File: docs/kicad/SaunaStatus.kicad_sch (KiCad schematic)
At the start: 9 parts, among them J1 PT1000-Connector, J2 28BYJ-48, J3 28BYJ-48, U1 ESP32-WROOM-32, U2 MAX31865xAP, U3 DHT21/AM2301, U4 DHT21/AM2301, U5 ULN2003A, U6 ULN2003A

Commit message: Replace INA219 power monitor with INA260 throughout
- src/main.cpp: swap Adafruit_INA219 → Adafruit_INA260; update include,
  defines (INA219_* → INA260_*), object name (ina219 → ina260),
  init guard (ina219_ok → ina260_ok), and all read methods
  (getPowerW/getShuntVoltage_mV → readPower/readCurrent/readBusVoltage)
- platformio.ini: replace INA219 library with
  adafruit/Adafruit INA260 Library@^1.5.3
- docs/hardware-rules.md: update Pin Table, Section 3 (I2C Bus),
  Section 7 (Power Monitor), constraint #9, Section 11 sauna note,
  and Schematic Component Reference table (U7 entry)
- docs/config-reference.md: rename INA219_SDA/SCL → INA260_SDA/SCL
- docs/api-reference.md: update pvolt/pcurr/pmw descriptions, MQTT
  field table, and InfluxDB sauna_status fields; fix gateway to 192.168.1.100
- docs/pinout.md: add INA260 I2C wiring section; add GPIO 4/13 to
  Quick Reference table
- CLAUDE.md: update project overview, Sensor Layer table,
  WebSocket JSON schema, and InfluxDB field descriptions
- docs/kicad/SaunaStatus.kicad_sch: add INA260 (U7, TSSOP-16) component

INA260 wiring: SDA=GPIO4, SCL=GPIO13, A0=A1=GND (I2C address 0x40).
Integrated 2 mΩ shunt — no external shunt resistor required.
U7 is placed in the schematic but not yet wired; connections must be
routed in the next PCB revision.

Co-Authored-By: Claude Sonnet 4.6 <noreply@anthropic.com>
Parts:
- added U7: INA260, Package_SO:TSSOP-16_4.4x5mm_P0.65mm, symbol Sensor:INA260
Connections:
- new net: U7.1 (IN+), U7.2 (IN+), U7.3 (IN+)
- new net: U7.11 (GND), U7.6 (GND)
- new net: U7.14 (IN-), U7.15 (IN-), U7.16 (IN-)
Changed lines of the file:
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@@
+	)
+	(symbol
+		(lib_id "Sensor:INA260")
+		(at 223.52 172.72 0)
+		(unit 1)
+		(exclude_from_sim no)
+		(in_bom yes)
+		(on_board yes)
+		(dnp no)
+		(fields_autoplaced yes)
+		(property "Reference" "U7"
+			(at 225.6633 160.02 0)
+			(effects
+				(font
+					(size 1.27 1.27)
+				)
+				(justify left)
+			)
+		)
+		(property "Value" "INA260"
+			(at 225.6633 162.56 0)
+			(effects
+				(font
+					(size 1.27 1.27)
+				)
+				(justify left)
+			)
+		)
+		(property "Footprint" "Package_SO:TSSOP-16_4.4x5mm_P0.65mm"
+			(at 223.52 187.96 0)
+			(effects
+				(font
+					(size 1.27 1.27)
+				)
+				(hide yes)
+			)
+		)
+		(property "Datasheet" "http://www.ti.com/lit/ds/symlink/ina260.pdf"
+			(at 223.52 175.26 0)
+			(effects
+				(font
+					(size 1.27 1.27)
+				)
+				(hide yes)
+			)
+		)
+		(property "Description" "Current/power/voltage monitor with Integrated 2mΩ Shunt Resistor, 2.7V - 5.5V, I2C, TSSOP-16"
+			(at 223.52 172.72 0)
+			(effects
+				(font
+					(size 1.27 1.27)
+				)
+				(hide yes)
+			)
+		)
+		(pin "4"
+		)
+		(pin "9"
+		)
+		(pin "12"
+		)
+		(pin "14"
+		)
+		(pin "15"
+		)
+		(pin "16"
+		)
+		(pin "7"
+		)
+		(pin "6"
+		)
+		(pin "10"
+		)
+		(pin "3"
+		)
+		(pin "2"
+		)
+		(pin "1"
+		)
+		(pin "8"
+		)
+		(pin "5"
+		)
+		(pin "13"
+		)
+		(pin "11"
+		)
+		(instances
+			(project "SaunaStatus"
+				(path "/d19a36c6-5583-4c95-873e-3cdaa80a72d5"
+					(reference "U7")
+					(unit 1)
+				)
+			)
+		)
 	)
 	(symbol

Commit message: feat(kicad): replace DHT21 sensor footprints with J4/J5 connectors
Sensors are external packages; replace U3/U4 (wrong Sensor:DHT11
footprint) with Conn_01x04 connectors matching AM2301 pinout directly:
Pin1=VDD, Pin2=DATA, Pin3=NC, Pin4=GND.

Also wire INA260 (U7): I2C_SDA/SCL to ESP32 IO4/IO13, VS→+3V3, GND,
A0/A1→GND (address 0x40), VBUS→IN+, INA_IN+/- labels for sense path.

Update PCB footprints, CLAUDE.md, and docs/pinout.md accordingly.

Co-Authored-By: Claude Sonnet 4.6 <noreply@anthropic.com>
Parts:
- removed U3, U4: DHT21/AM2301, Sensor:Aosong_DHT11_5.5x12.0_P2.54mm, symbol Sensor:DHT11
- added J4: DHT21/AM2301 Ceiling, Connector_PinHeader_2.54mm:PinHeader_1x04_P2.54mm_Vertical, symbol Connector_Generic:Conn_01x04
- added J5: DHT21/AM2301 Bench, Connector_PinHeader_2.54mm:PinHeader_1x04_P2.54mm_Vertical, symbol Connector_Generic:Conn_01x04
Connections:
- net +3V3: now also U7.10 (VS)
- net DHT_BENCH: now also J5.2 (Pin_2)
- net DHT_CEILING: now also J4.2 (Pin_2)
- net GND: now also U7.11 (GND), U7.4 (A1), U7.5 (A0), U7.6 (GND)
- net U6_28BYJ_A: no longer J3.1 (Pin_1), U6.16 (O1)
- net U6_28BYJ_B: no longer J3.2 (Pin_2), U6.15 (O2)
- net I2C_SCL: now reaches U1.16 (IO13)
- net I2C_SCL: now also U7.9 (SCL)
- net I2C_SDA: now reaches U1.26 (IO4)
- net I2C_SDA: now also U7.8 (SDA)
- net INA_IN+: now reaches U7.1 (IN+), U7.2 (IN+), U7.3 (IN+)
- net INA_IN+: now also U7.12 (VBUS)
- net INA_IN-: now reaches U7.14 (IN-), U7.15 (IN-), U7.16 (IN-)
- no-connect marks 36 -> 37

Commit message: fix(kicad): resolve ERC/DRC errors — wire J4/J5 power pins, U6 outputs, add board outline
ERC fixes (16 errors → expected 4 or fewer):
- J4 (DHT Ceiling connector): add +3V3→Pin1 and Pin4→GND wires
- J5 (DHT Bench connector): add +3V3→Pin1 and Pin4→GND wires
- Remove two dangling data-stub wires left from DHT21→connector replacement
- U6 O1/O2: add wires (162.56→182.88mm) connecting Pin16/15 to J3 Pin1/2
  via U6_28BYJ_A/B labels — mirrors the working C/D pattern

DRC fix:
- Add Edge.Cuts board outline (gr_rect 67,55 → 220,130mm) — no outline existed

Remaining DRC items require KiCad GUI:
- 49 unconnected pads: PCB has 0 routed traces, full layout required
- SSOP-20 (MAX31865) clearance violations: inherent to 0.65mm pitch, use local override
- ESP32 thermal pad 0.2mm vias: violate 0.3mm default min-drill; select fab supporting micro-vias
- Library footprint mismatches: warnings only, accept or re-sync from library

gitignore: add docs/kicad/*.rpt (ERC/DRC reports are generated, not source-controlled)

Co-Authored-By: Claude Sonnet 4.6 <noreply@anthropic.com>
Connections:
- net +3V3: now also J4.1 (Pin_1), J5.1 (Pin_1)
- net GND: now also J4.4 (Pin_4), J5.4 (Pin_4)
- net U6_28BYJ_A: now also J3.1 (Pin_1), U6.16 (O1)
- net U6_28BYJ_B: now also J3.2 (Pin_2), U6.15 (O2)
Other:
- moved on the sheet: J4, J5

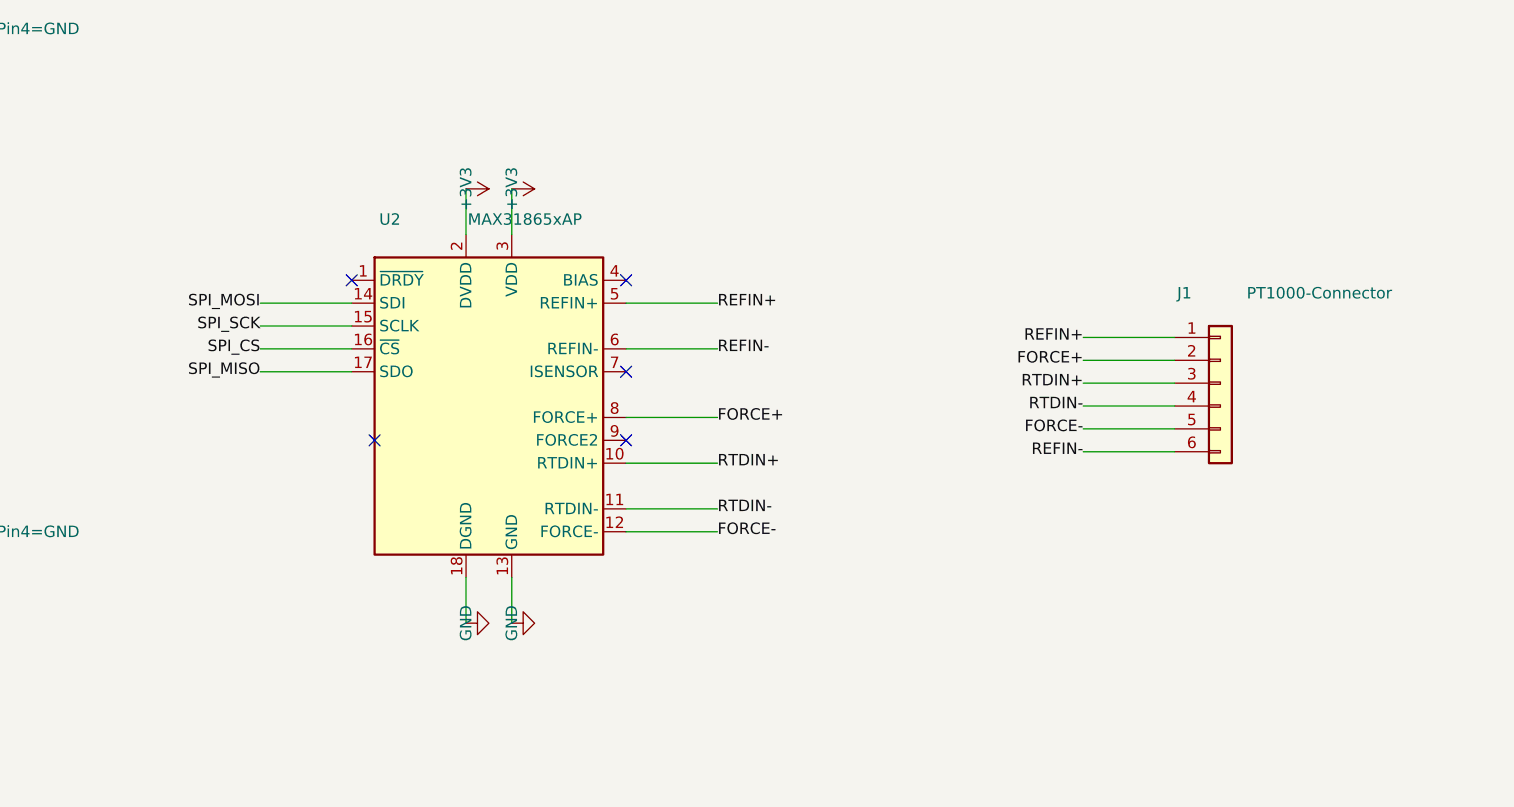
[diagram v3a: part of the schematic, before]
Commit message: feat(kicad): replace MAX31865 bare IC with Adafruit breakout connector
Remove U2 (MAX31865xAP SSOP-20) and J1 (6-pin PT1000 connector);
replace with J1 (Conn_01x08) for Adafruit MAX31865 breakout board.
SPI GPIO assignments unchanged (CS=5, SCK=18, MISO=19, MOSI=23).

Pin mapping on new J1:
  1=VIN(+3V3)  2=3Vo(NC)  3=GND  4=CLK(SPI_SCK)
  5=SDO(SPI_MISO)  6=SDI(SPI_MOSI)  7=CS(SPI_CS)  8=RDY(NC)

Remove 6 stale RTD net declarations from PCB (RTDIN+/-, FORCE+/-,
REFIN+/-). DRC improved from 34 to 16 violations (all pre-existing).
All 113 native unit tests pass.

Hardware prerequisite: set Adafruit breakout 3-wire solder jumper
before installation (ships in 2-wire/4-wire mode by default).

Co-Authored-By: Claude Sonnet 4.6 <noreply@anthropic.com>
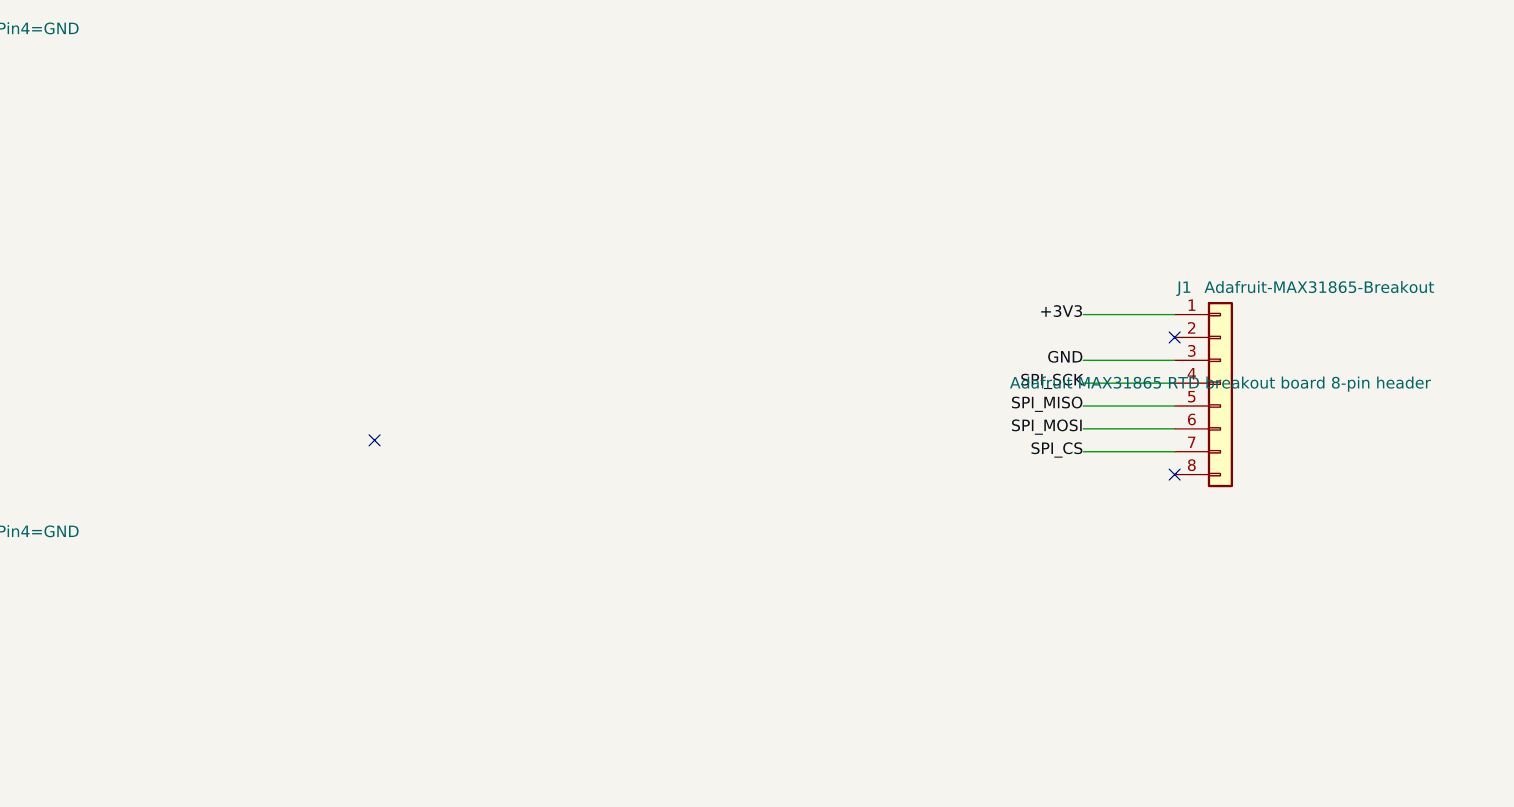
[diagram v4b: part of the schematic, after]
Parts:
- removed J1: PT1000-Connector, Connector_PinHeader_2.54mm:PinHeader_1x06_P2.54mm_Vertical, symbol Connector_Generic:Conn_01x06
- removed U2: MAX31865xAP, Package_SO:SSOP-20_5.3x7.2mm_P0.65mm, symbol Sensor_Temperature:MAX31865xAP
- added J1: Adafruit-MAX31865-Breakout, Connector_PinHeader_2.54mm:PinHeader_1x08_P2.54mm_Vertical, symbol Connector_Generic:Conn_01x08
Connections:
- net +3V3: now also J1.1 (Pin_1)
- net GND: now also J1.3 (Pin_3)
- net SPI_CS: now also J1.7 (Pin_7)
- net SPI_MISO: now also J1.5 (Pin_5)
- net SPI_MOSI: now also J1.6 (Pin_6)
- net SPI_SCK: now also J1.4 (Pin_4)
- no-connect marks 37 -> 35
